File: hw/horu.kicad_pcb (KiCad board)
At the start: 4 copper layers, 40.3 x 54.2 mm, 37 parts, among them P1 CONN_01X06, P2 USB_OTG, P3 CONN_01X30_2SHIELD, P4 CONN_01X06, P5 CONN_02X05, U1 KL25P80M48SF0, Y1 8MHz

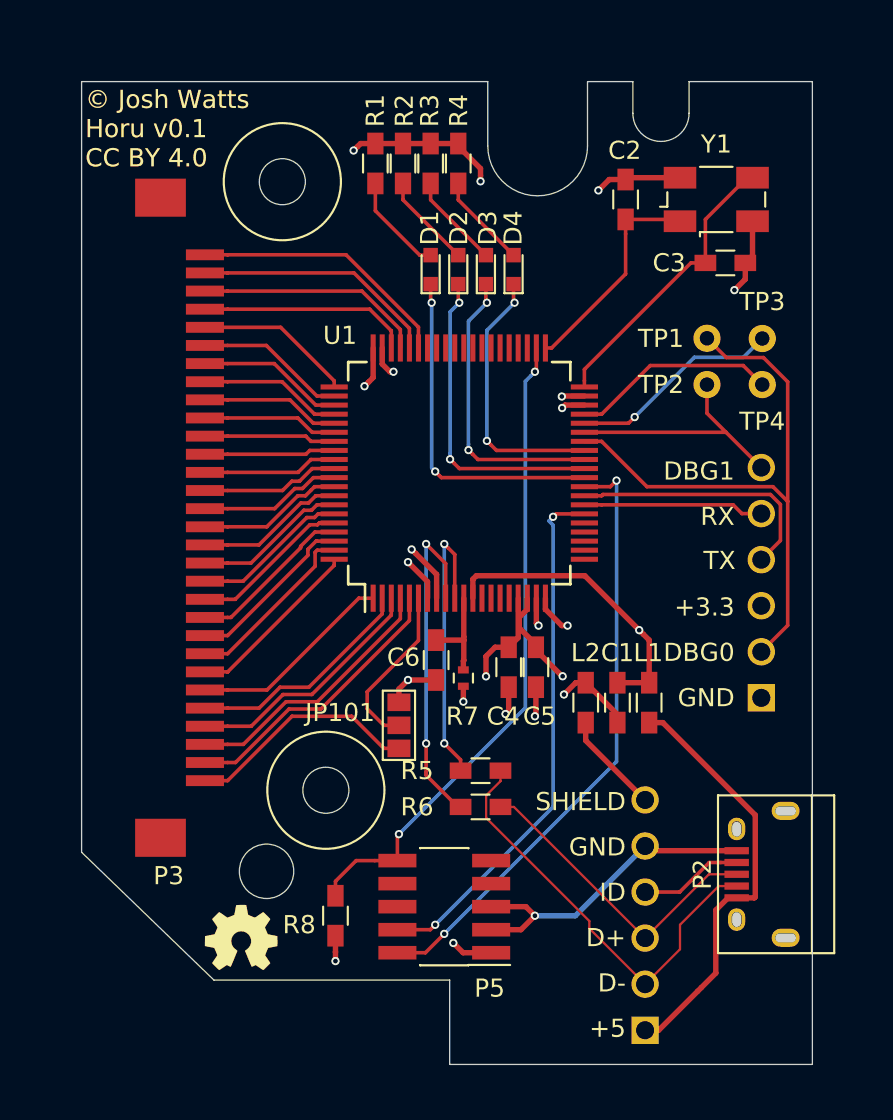
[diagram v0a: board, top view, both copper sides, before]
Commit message: Changed to copper pour for each layer
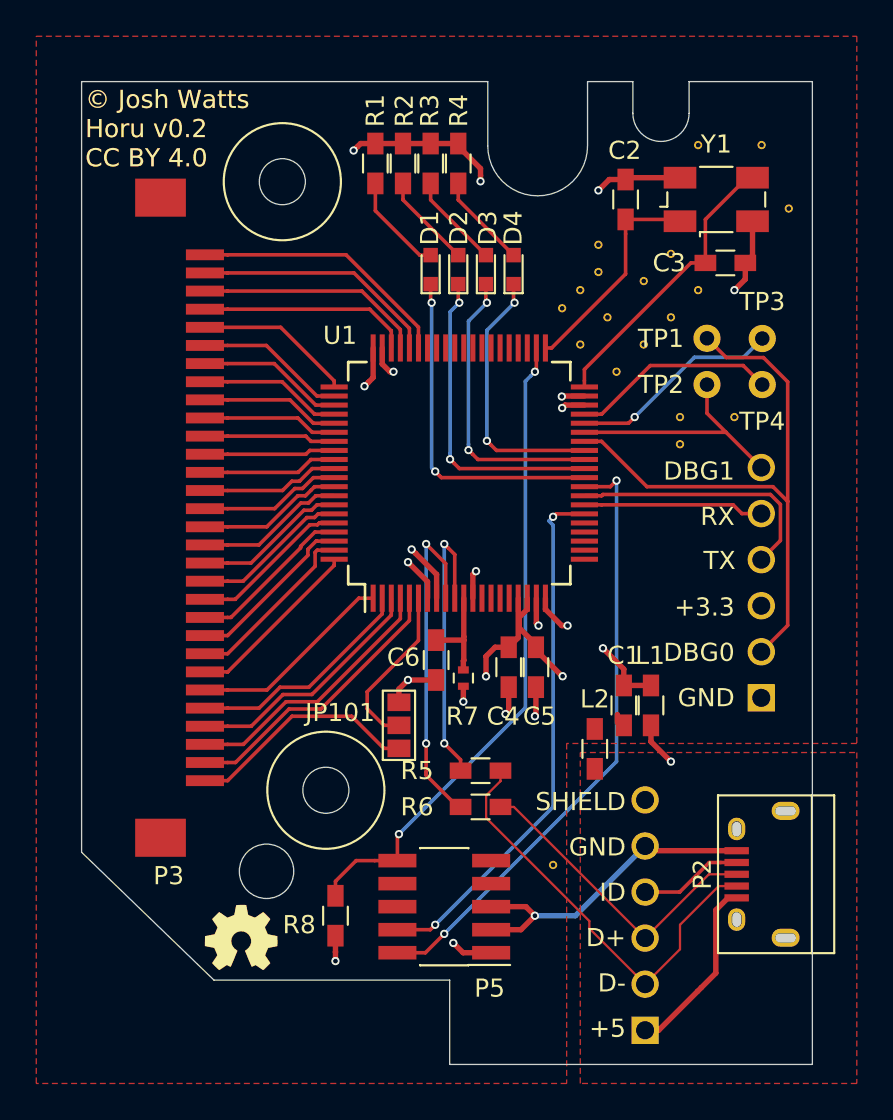
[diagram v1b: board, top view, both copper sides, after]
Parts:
- added REF**: VIA-0.4572mm, horu:VIA-0.4572mm, F.Cu at (86.0, 103.2)
- added REF**: VIA-0.4572mm, horu:VIA-0.4572mm, F.Cu at (87.5, 71.5)
- added REF**: VIA-0.4572mm, horu:VIA-0.4572mm, F.Cu at (88.5, 70.5)
- added REF**: VIA-0.4572mm, horu:VIA-0.4572mm, F.Cu at (88.5, 69.0)
- added REF**: VIA-0.4572mm, horu:VIA-0.4572mm, F.Cu at (92.5, 69.5)
- added REF**: VIA-0.4572mm, horu:VIA-0.4572mm, F.Cu at (91.0, 71.0)
- added REF**: VIA-0.4572mm, horu:VIA-0.4572mm, F.Cu at (89.0, 73.0)
- added REF**: VIA-0.4572mm, horu:VIA-0.4572mm, F.Cu at (87.5, 74.5)
- added REF**: VIA-0.4572mm, horu:VIA-0.4572mm, F.Cu at (96.0, 78.5)
- added REF**: VIA-0.4572mm, horu:VIA-0.4572mm, F.Cu at (93.0, 80.0)
- added REF**: VIA-0.4572mm, horu:VIA-0.4572mm, F.Cu at (94.0, 63.5)
- added REF**: VIA-0.4572mm, horu:VIA-0.4572mm, F.Cu at (93.0, 78.5)
- added REF**: VIA-0.4572mm, horu:VIA-0.4572mm, F.Cu at (97.5, 63.5)
- added REF**: VIA-0.4572mm, horu:VIA-0.4572mm, F.Cu at (99.0, 67.0)
- added REF**: VIA-0.4572mm, horu:VIA-0.4572mm, F.Cu at (94.0, 71.5)
- added REF**: VIA-0.4572mm, horu:VIA-0.4572mm, F.Cu at (92.5, 73.0)
- added REF**: VIA-0.4572mm, horu:VIA-0.4572mm, F.Cu at (91.0, 74.5)
- added REF**: VIA-0.4572mm, horu:VIA-0.4572mm, F.Cu at (89.5, 76.0)
- added REF**: VIA-0.4572mm, horu:VIA-0.4572mm, F.Cu at (86.5, 72.5)
- moved L2 2.60 mm to (88.3, 96.8)
- moved C1 0.38 mm to (89.9, 94.4)
- moved L1 0.18 mm to (91.4, 94.4)
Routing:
- net /USB_SHIELD: track 5.62 -> 17.1 mm
- net /USB_VBUS: track 23.6 -> 28.3 mm, vias 0 -> 1
- net GND: track 60.6 -> 56.6 mm, vias 12 -> 11
- net VUSB: track 16.4 -> 14.5 mm, vias 1 -> 2
- net +3V3_SDA: track 124.3 -> 125.5 mm
- added copper zone on In1.Cu, net +3V3_SDA
- added copper zone on F.Cu, net /USB_SHIELD
- added copper zone on In1.Cu, net /USB_VBUS
- added copper zone on F.Cu, net GND
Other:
- board text added: "© Josh Watts Horu v0.2 CC BY 4.0"
- board text removed: "© Josh Watts Horu v0.1 CC BY 4.0"

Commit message: Update schematic and prepare for release
* Update rev to v1.0
* Update USB_OTG symbol
* Add missing USB ESD diodes
* Fill in manf# for all parts
* Export BOM using kicost
* Fill ground on bottom layer
* Replace traces on inner 2 with properly placed vias to allow fill to connect everything
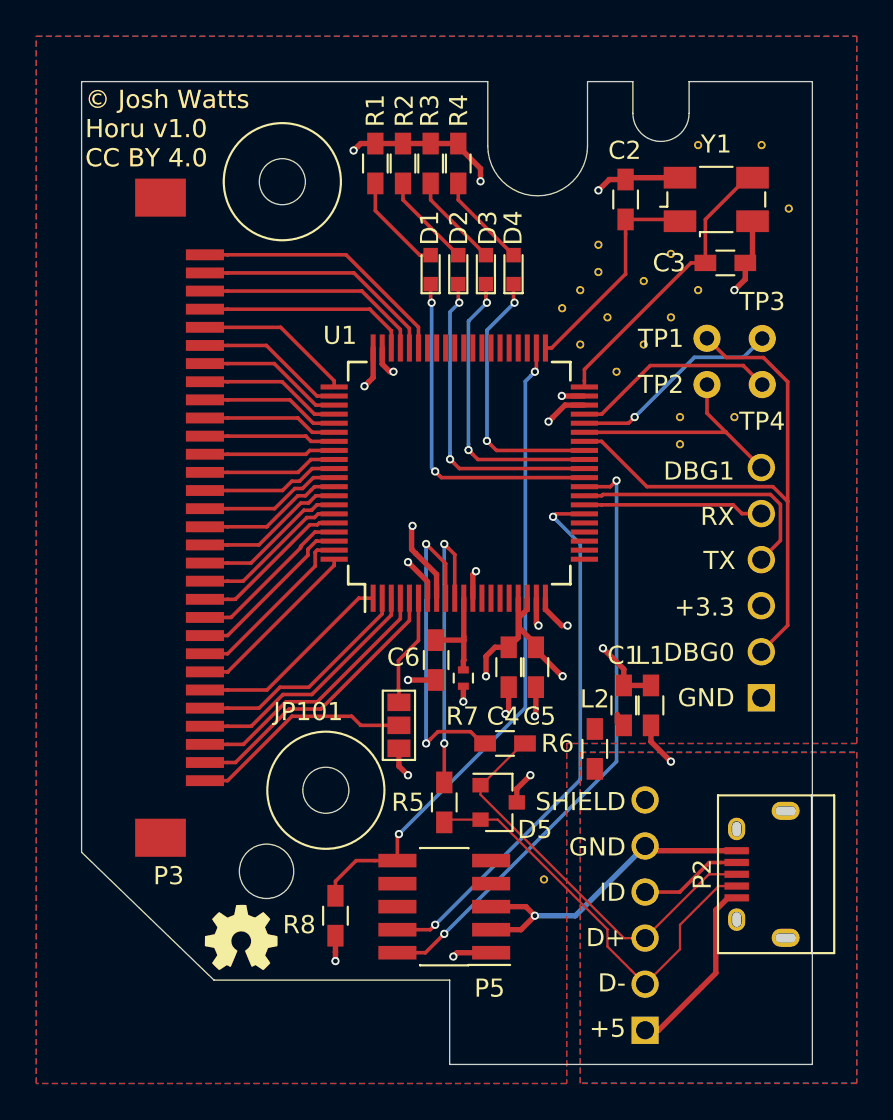
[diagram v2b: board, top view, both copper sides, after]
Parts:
- added D5: D_Zener_x2_ACom_KKA, TO_SOT_Packages_SMD:SOT-23, F.Cu at (83.0, 99.8)
- moved R6 3.75 mm to (83.3, 96.5)
- moved R5 2.66 mm to (80.0, 99.8), turned to 270 degrees
- moved REF** 0.94 mm to (85.5, 104.0)
- turned JP101 to 0 degrees
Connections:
- JP101 pad 1: /CON30 -> /MCU_CON30
- JP101 pad 2: /MCU_CON30 -> /CON30
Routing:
- net +3V3_SDA: track 125.5 -> 31.4 mm
- net /USB_VBUS: track 28.3 -> 12.6 mm
- net /USB_D+: track 17.5 -> 23.1 mm
- net GND: track 56.6 -> 60.0 mm, vias 11 -> 13
- net /MCU_CON30: track 9.40 -> 6.21 mm
- net /SWD_DIO: track 29.4 -> 30.4 mm
- net /MCU_USB_D+: track 18.8 -> 18.2 mm
- net /CON30: track 12.9 -> 12.4 mm
- added copper zone on B.Cu, net /USB_SHIELD
- added copper zone on B.Cu, net GND
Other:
- board text added: "© Josh Watts Horu v1.0 CC BY 4.0"
- board text removed: "© Josh Watts Horu v0.2 CC BY 4.0"

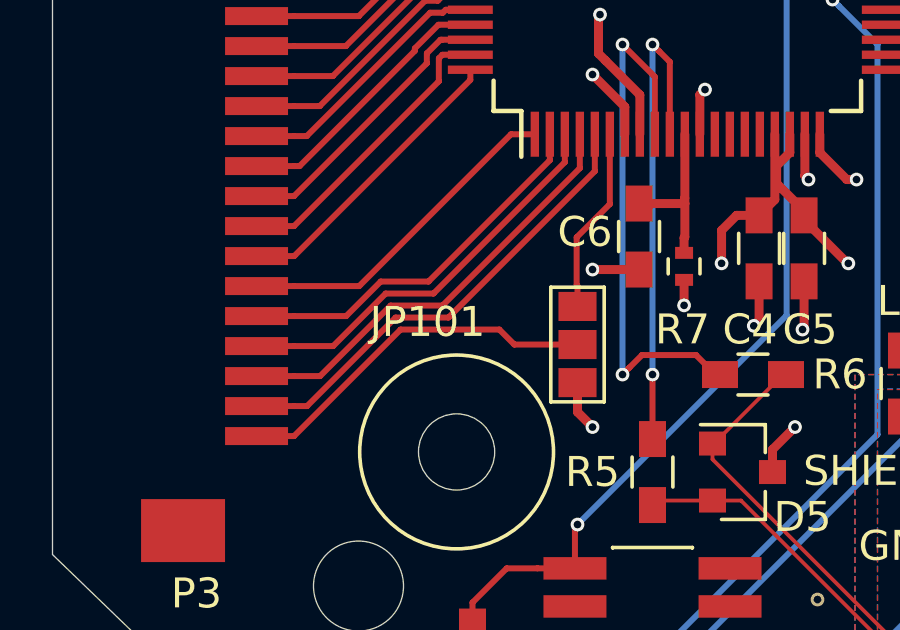
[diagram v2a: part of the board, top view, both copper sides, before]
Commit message: Update design
* Fix JP101 -> JP1
* Update USB_OTG -> DNP
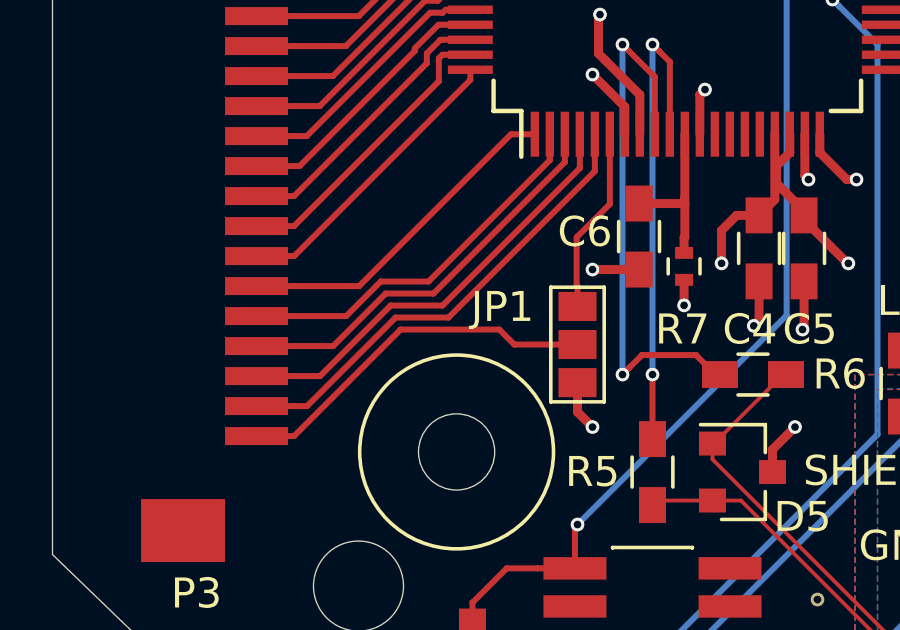
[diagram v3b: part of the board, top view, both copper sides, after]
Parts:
- removed JP101: Jumper_NC_Dual, Connectors:GS3
- added JP1: Jumper_NC_Dual, Connectors:GS3, F.Cu at (77.5, 95.5)
- P2: value USB_OTG -> DNP
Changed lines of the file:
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@@
     (links 128)
     (no_connects 0)
-    (area 57.5 57.5 104.866666 115.250001)
+    (area 59.987299 59.987299 100.312701 114.212701)
     (thickness 1.6)
     (drawings 33)
@@
   (layers
     (0 F.Cu signal)
-    (1 In1.Cu power)
-    (2 In2.Cu power)
-    (31 B.Cu signal)
+    (1 In1.Cu power hide)
+    (2 In2.Cu power hide)
+    (31 B.Cu signal hide)
     (33 F.Adhes user hide)
     (35 F.Paste user hide)
@@
       (effects (font (size 1 1) (thickness 0.15)))
     )
-    (fp_text value USB_OTG (at 0 5.01 90) (layer F.Fab)
+    (fp_text value DNP (at 0 5.01 90) (layer F.Fab)
       (effects (font (size 1 1) (thickness 0.15)))
     )
@@
       (net 15 /USB_SHIELD))
   )
-  (module Connectors:GS3 (layer F.Cu)
-    (at 77.5 95.5)
-    (descr "3-pin solder bridge")
-    (tags "solder bridge")
-    (attr smd)
-    (fp_text reference JP101 (at -5 -0.75) (layer F.SilkS)
-      (effects (font (size 1 1) (thickness 0.15)))
-    )
-    (fp_text value Jumper_NC_Dual (at 1.8 0 90) (layer F.Fab)
-      (effects (font (size 1 1) (thickness 0.15)))
-    )
-    (fp_line (start -1.15 -2.15) (end 1.15 -2.15) (layer F.CrtYd) (width 0.05))
-    (fp_line (start 1.15 -2.15) (end 1.15 2.15) (layer F.CrtYd) (width 0.05))
-    (fp_line (start 1.15 2.15) (end -1.15 2.15) (layer F.CrtYd) (width 0.05))
-    (fp_line (start -1.15 2.15) (end -1.15 -2.15) (layer F.CrtYd) (width 0.05))
-    (fp_line (start -0.89 -1.91) (end -0.89 1.91) (layer F.SilkS) (width 0.12))
-    (fp_line (start -0.89 1.91) (end 0.89 1.91) (layer F.SilkS) (width 0.12))
-    (fp_line (start 0.89 1.91) (end 0.89 -1.91) (layer F.SilkS) (width 0.12))
-    (fp_line (start -0.89 -1.91) (end 0.89 -1.91) (layer F.SilkS) (width 0.12))
-    (pad 1 smd rect (at 0 -1.27) (size 1.27 0.97) (layers F.Cu F.Paste F.Mask)
-      (net 67 /MCU_CON30))
-    (pad 2 smd rect (at 0 0) (size 1.27 0.97) (layers F.Cu F.Paste F.Mask)
-      (net 61 /CON30))
-    (pad 3 smd rect (at 0 1.27) (size 1.27 0.97) (layers F.Cu F.Paste F.Mask)
-      (net 2 GND))
-  )
   (module horu:OSHW_F.Cu (layer F.Cu)
     (at 68.8 107.2)
@@
     )
   )
+  (module Connectors:GS3 (layer F.Cu)
+    (at 77.5 95.5)
+    (descr "3-pin solder bridge")
+    (tags "solder bridge")
+    (attr smd)
+    (fp_text reference JP1 (at -2.5 -1.25) (layer F.SilkS)
+      (effects (font (size 1 1) (thickness 0.15)))
+    )
+    (fp_text value Jumper_NC_Dual (at 1.8 0 90) (layer F.Fab)
+      (effects (font (size 1 1) (thickness 0.15)))
+    )
+    (fp_line (start -1.15 -2.15) (end 1.15 -2.15) (layer F.CrtYd) (width 0.05))
+    (fp_line (start 1.15 -2.15) (end 1.15 2.15) (layer F.CrtYd) (width 0.05))
+    (fp_line (start 1.15 2.15) (end -1.15 2.15) (layer F.CrtYd) (width 0.05))
+    (fp_line (start -1.15 2.15) (end -1.15 -2.15) (layer F.CrtYd) (width 0.05))
+    (fp_line (start -0.89 -1.91) (end -0.89 1.91) (layer F.SilkS) (width 0.12))
+    (fp_line (start -0.89 1.91) (end 0.89 1.91) (layer F.SilkS) (width 0.12))
+    (fp_line (start 0.89 1.91) (end 0.89 -1.91) (layer F.SilkS) (width 0.12))
+    (fp_line (start -0.89 -1.91) (end 0.89 -1.91) (layer F.SilkS) (width 0.12))
+    (pad 1 smd rect (at 0 -1.27) (size 1.27 0.97) (layers F.Cu F.Paste F.Mask)
+      (net 67 /MCU_CON30))
+    (pad 2 smd rect (at 0 0) (size 1.27 0.97) (layers F.Cu F.Paste F.Mask)
+      (net 61 /CON30))
+    (pad 3 smd rect (at 0 1.27) (size 1.27 0.97) (layers F.Cu F.Paste F.Mask)
+      (net 2 GND))
+  )
   (gr_line (start 96.125 101.3875) (end 96.125 101.0625) (layer Edge.Cuts) (width 0.5))
